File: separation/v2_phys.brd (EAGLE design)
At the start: 8 parts

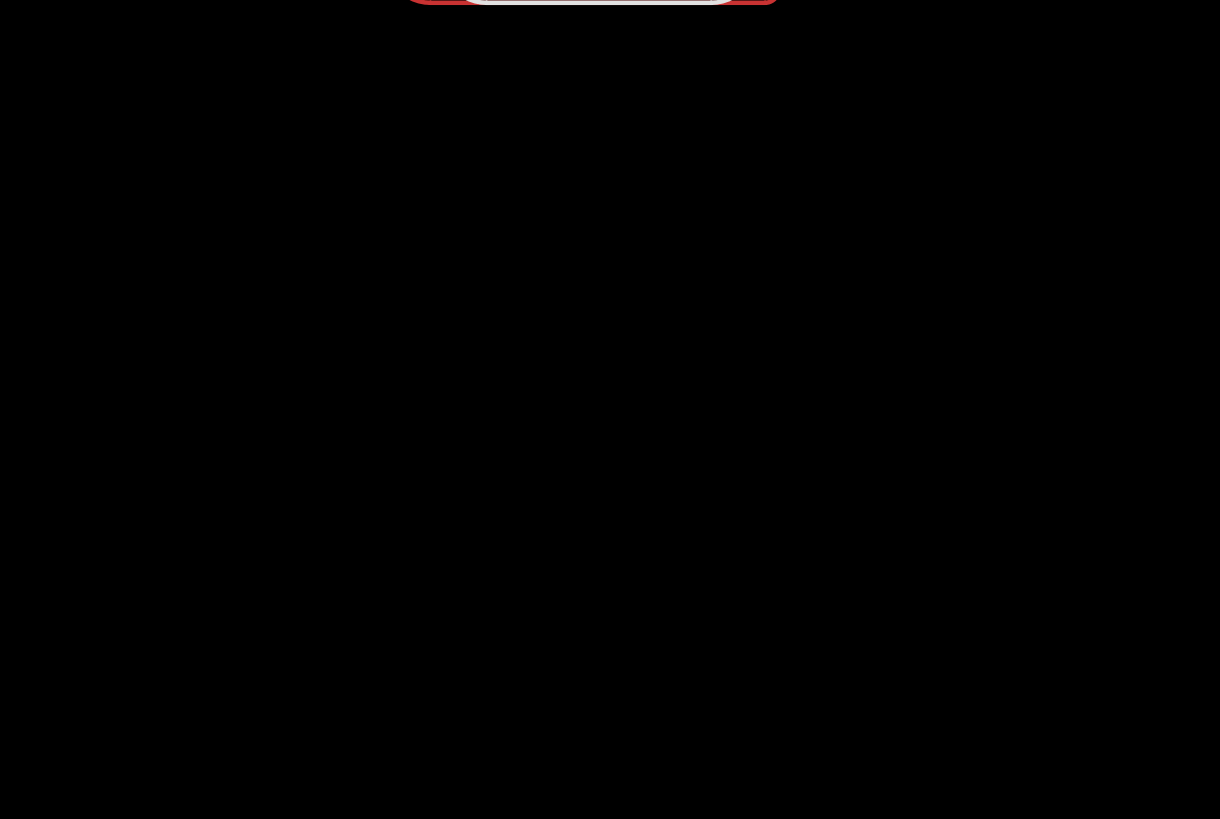
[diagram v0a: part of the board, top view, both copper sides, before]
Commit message: add 3x pressure sensors to physical model
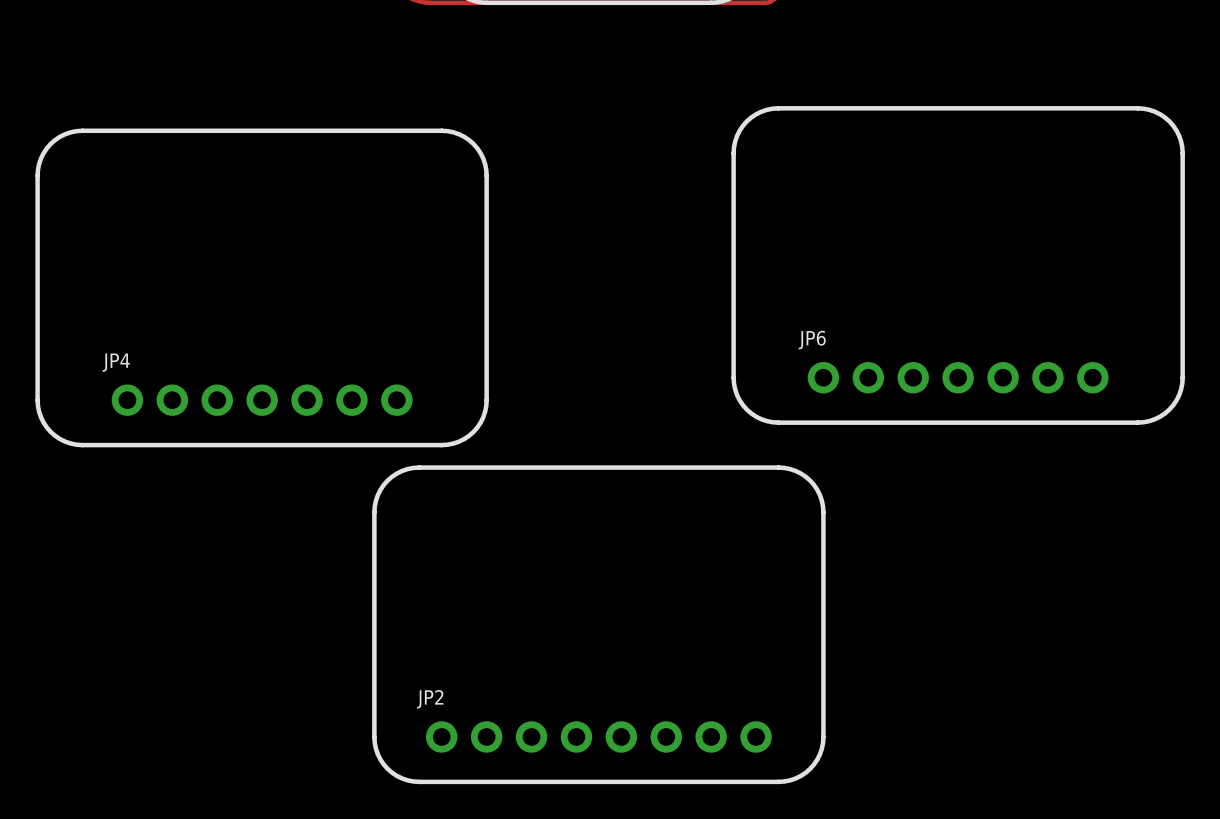
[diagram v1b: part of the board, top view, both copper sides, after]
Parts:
- added JP2: (no value), microbuilder:1X08_ROUND_70
- added JP4, JP6: (no value), microbuilder:1X07_ROUND_70
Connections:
- new net 3.3V: JP2.2, JP4.2, JP6.2
- new net CS: JP2.7, JP4.7, JP6.7
- new net INT: JP2.8
- new net SCK/SCL: JP2.4, JP4.4, JP6.4
- new net SDI/SDA: JP2.6, JP4.6, JP6.6
- new net SDO/ADR: JP2.5, JP4.5, JP6.5
- net GND: now also JP2.3, JP4.3, JP6.3
- net VCC: now also JP2.1, JP4.1, JP6.1
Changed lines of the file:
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@@
 <wire x1="-8.89" y1="26.543" x2="-10.668" y2="26.543" width="1.524" layer="29"/>
 <wire x1="-8.89" y1="29.083" x2="-10.668" y2="29.083" width="1.524" layer="29"/>
+<wire x1="-13.97" y1="-17.78" x2="-13.97" y2="-30.48" width="0.254" layer="21"/>
+<wire x1="-13.97" y1="-30.48" x2="-11.43" y2="-33.02" width="0.254" layer="21" curve="90"/>
+<wire x1="-11.43" y1="-33.02" x2="8.89" y2="-33.02" width="0.254" layer="21"/>
+<wire x1="8.89" y1="-33.02" x2="11.43" y2="-30.48" width="0.254" layer="21" curve="90"/>
+<wire x1="11.43" y1="-30.48" x2="11.43" y2="-17.78" width="0.254" layer="21"/>
+<wire x1="11.43" y1="-17.78" x2="8.89" y2="-15.24" width="0.254" layer="21" curve="90"/>
+<wire x1="8.89" y1="-15.24" x2="-11.43" y2="-15.24" width="0.254" layer="21"/>
+<wire x1="-11.43" y1="-15.24" x2="-13.97" y2="-17.78" width="0.254" layer="21" curve="90"/>
+<wire x1="-33.02" y1="1.27" x2="-33.02" y2="-11.43" width="0.254" layer="21"/>
+<wire x1="-33.02" y1="-11.43" x2="-30.48" y2="-13.97" width="0.254" layer="21" curve="90"/>
+<wire x1="-30.48" y1="-13.97" x2="-10.16" y2="-13.97" width="0.254" layer="21"/>
+<wire x1="-10.16" y1="-13.97" x2="-7.62" y2="-11.43" width="0.254" layer="21" curve="90"/>
+<wire x1="-7.62" y1="-11.43" x2="-7.62" y2="1.27" width="0.254" layer="21"/>
+<wire x1="-7.62" y1="1.27" x2="-10.16" y2="3.81" width="0.254" layer="21" curve="90"/>
+<wire x1="-10.16" y1="3.81" x2="-30.48" y2="3.81" width="0.254" layer="21"/>
+<wire x1="-30.48" y1="3.81" x2="-33.02" y2="1.27" width="0.254" layer="21" curve="90"/>
+<wire x1="6.35" y1="2.54" x2="6.35" y2="-10.16" width="0.254" layer="21"/>
+<wire x1="6.35" y1="-10.16" x2="8.89" y2="-12.7" width="0.254" layer="21" curve="90"/>
+<wire x1="8.89" y1="-12.7" x2="29.21" y2="-12.7" width="0.254" layer="21"/>
+<wire x1="29.21" y1="-12.7" x2="31.75" y2="-10.16" width="0.254" layer="21" curve="90"/>
+<wire x1="31.75" y1="-10.16" x2="31.75" y2="2.54" width="0.254" layer="21"/>
+<wire x1="31.75" y1="2.54" x2="29.21" y2="5.08" width="0.254" layer="21" curve="90"/>
+<wire x1="29.21" y1="5.08" x2="8.89" y2="5.08" width="0.254" layer="21"/>
+<wire x1="8.89" y1="5.08" x2="6.35" y2="2.54" width="0.254" layer="21" curve="90"/>
 </plain>
 <attributes>
@@
 <class number="0" name="default" width="0" drill="0">
 </class>
-<class number="1" name="power" width="0.3048" drill="0">
+<class number="1" name="highpower" width="0.3048" drill="0.4826">
+</class>
+<class number="2" name="lowpower" width="0.3048" drill="0.4826">
 </class>
 </classes>
@@
 <attribute name="VALUE" x="8.1534" y="31.1404" size="0.9906" layer="27" ratio="10"/>
 </element>
+<element name="JP2" library="microbuilder" package="1X08_ROUND_70" value="" x="-1.27" y="-30.48" smashed="yes">
+<attribute name="NAME" x="-11.5062" y="-28.6512" size="0.8128" layer="25" ratio="18"/>
+<attribute name="VALUE" x="-11.43" y="-33.655" size="0.4064" layer="27" ratio="10"/>
+</element>
+<element name="JP4" library="microbuilder" package="1X07_ROUND_70" value="" x="-20.32" y="-11.43" smashed="yes">
+<attribute name="NAME" x="-29.2862" y="-9.6012" size="0.8128" layer="25" ratio="18"/>
+<attribute name="VALUE" x="-29.21" y="-14.605" size="0.4064" layer="27" ratio="10"/>
+</element>
+<element name="JP6" library="microbuilder" package="1X07_ROUND_70" value="" x="19.05" y="-10.16" smashed="yes">
+<attribute name="NAME" x="10.0838" y="-8.3312" size="0.8128" layer="25" ratio="18"/>
+<attribute name="VALUE" x="10.16" y="-13.335" size="0.4064" layer="27" ratio="10"/>
+</element>
 </elements>
 <signals>
@@
 <contactref element="LOUD" pad="2"/>
 <contactref element="R2" pad="2"/>
+<contactref element="JP2" pad="3"/>
+<contactref element="JP4" pad="3"/>
+<contactref element="JP6" pad="3"/>
+<wire x1="11.303" y1="27.051" x2="14.097" y2="22.931" width="0" layer="19" extent="1-1"/>
 <wire x1="13.97" y1="13.97" x2="14.097" y2="22.931" width="0" layer="19" extent="1-1"/>
-<wire x1="-17.79" y1="17.018" x2="13.97" y2="13.97" width="0" layer="19" extent="1-1"/>
+<wire x1="-8.89" y1="16.3195" x2="11.303" y2="27.051" width="0" layer="19" extent="1-1"/>
+<wire x1="-17.79" y1="17.018" x2="-8.89" y2="16.3195" width="0" layer="19" extent="1-1"/>
 <wire x1="-17.78" y1="22.67" x2="-17.79" y2="17.018" width="0" layer="19" extent="1-1"/>
-<wire x1="11.303" y1="27.051" x2="-17.78" y2="22.67" width="0" layer="19" extent="1-1"/>
-<wire x1="-8.89" y1="16.3195" x2="11.303" y2="27.051" width="0" layer="19" extent="1-1"/>
+<wire x1="16.51" y1="-10.16" x2="13.97" y2="13.97" width="0" layer="19" extent="1-1"/>
+<wire x1="-22.86" y1="-11.43" x2="-17.79" y2="17.018" width="0" layer="19" extent="1-1"/>
+<wire x1="-5.08" y1="-30.48" x2="-22.86" y2="-11.43" width="0" layer="19" extent="1-1"/>
 </signal>
 <signal name="MOSI">
@@
 <wire x1="-20.32" y1="15.24" x2="-18.8595" y2="13.7795" width="0.508" layer="16" curve="90"/>
 <wire x1="-18.8595" y1="13.7795" x2="-8.89" y2="13.7795" width="0.508" layer="16"/>
+<contactref element="JP2" pad="1"/>
+<contactref element="JP4" pad="1"/>
+<contactref element="JP6" pad="1"/>
+<wire x1="-27.94" y1="-11.43" x2="-10.16" y2="-30.48" width="0" layer="19" extent="1-1"/>
+<wire x1="-20.34" y1="17.018" x2="-27.94" y2="-11.43" width="0" layer="19" extent="1-1"/>
+<wire x1="11.43" y1="-10.16" x2="-10.16" y2="-30.48" width="0" layer="19" extent="1-1"/>
 </signal>
 <signal name="+3V3">
@@
 <wire x1="9.652" y1="28.829" x2="9.652" y2="19.812" width="0.254" layer="1"/>
 </signal>
+<signal name="3.3V">
+<contactref element="JP2" pad="2"/>
+<contactref element="JP4" pad="2"/>
+<contactref element="JP6" pad="2"/>
+<wire x1="-25.4" y1="-11.43" x2="-7.62" y2="-30.48" width="0" layer="19" extent="1-1"/>
+<wire x1="13.97" y1="-10.16" x2="-7.62" y2="-30.48" width="0" layer="19" extent="1-1"/>
+</signal>
+<signal name="SDO/ADR">
+<contactref element="JP2" pad="5"/>
+<contactref element="JP4" pad="5"/>
+<contactref element="JP6" pad="5"/>
+<wire x1="-17.78" y1="-11.43" x2="0" y2="-30.48" width="0" layer="19" extent="1-1"/>
+<wire x1="21.59" y1="-10.16" x2="0" y2="-30.48" width="0" layer="19" extent="1-1"/>
+</signal>
+<signal name="SDI/SDA">
+<contactref element="JP2" pad="6"/>
+<contactref element="JP4" pad="6"/>
+<contactref element="JP6" pad="6"/>
+<wire x1="-15.24" y1="-11.43" x2="2.54" y2="-30.48" width="0" layer="19" extent="1-1"/>
+<wire x1="24.13" y1="-10.16" x2="2.54" y2="-30.48" width="0" layer="19" extent="1-1"/>
+</signal>
+<signal name="SCK/SCL">
+<contactref element="JP2" pad="4"/>
+<contactref element="JP4" pad="4"/>
+<contactref element="JP6" pad="4"/>
+<wire x1="-20.32" y1="-11.43" x2="-2.54" y2="-30.48" width="0" layer="19" extent="1-1"/>
+<wire x1="19.05" y1="-10.16" x2="-2.54" y2="-30.48" width="0" layer="19" extent="1-1"/>
+</signal>
+<signal name="CS">
+<contactref element="JP2" pad="7"/>
+<contactref element="JP4" pad="7"/>
+<contactref element="JP6" pad="7"/>
+<wire x1="-12.7" y1="-11.43" x2="5.08" y2="-30.48" width="0" layer="19" extent="1-1"/>
+<wire x1="26.67" y1="-10.16" x2="5.08" y2="-30.48" width="0" layer="19" extent="1-1"/>
+</signal>
+<signal name="INT">
+<contactref element="JP2" pad="8"/>
+</signal>
 </signals>

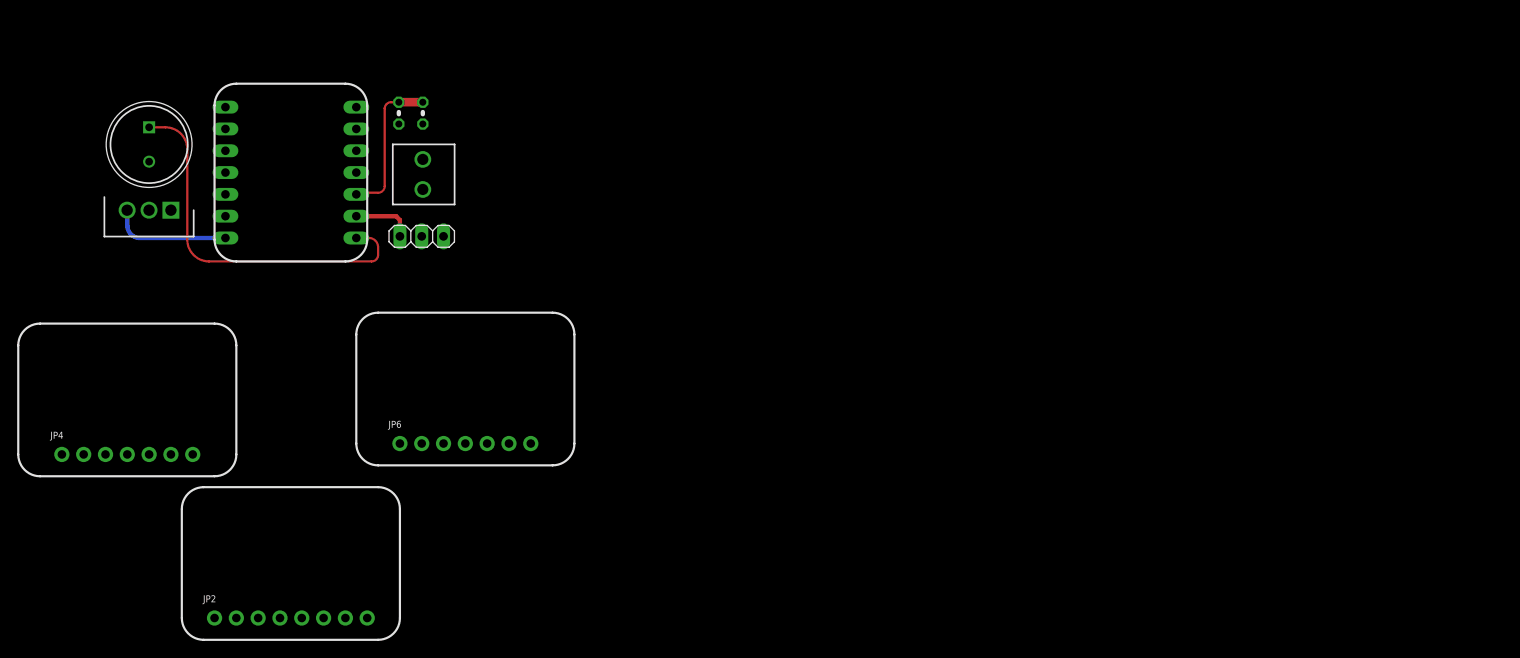
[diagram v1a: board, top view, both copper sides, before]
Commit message: possible physical layout
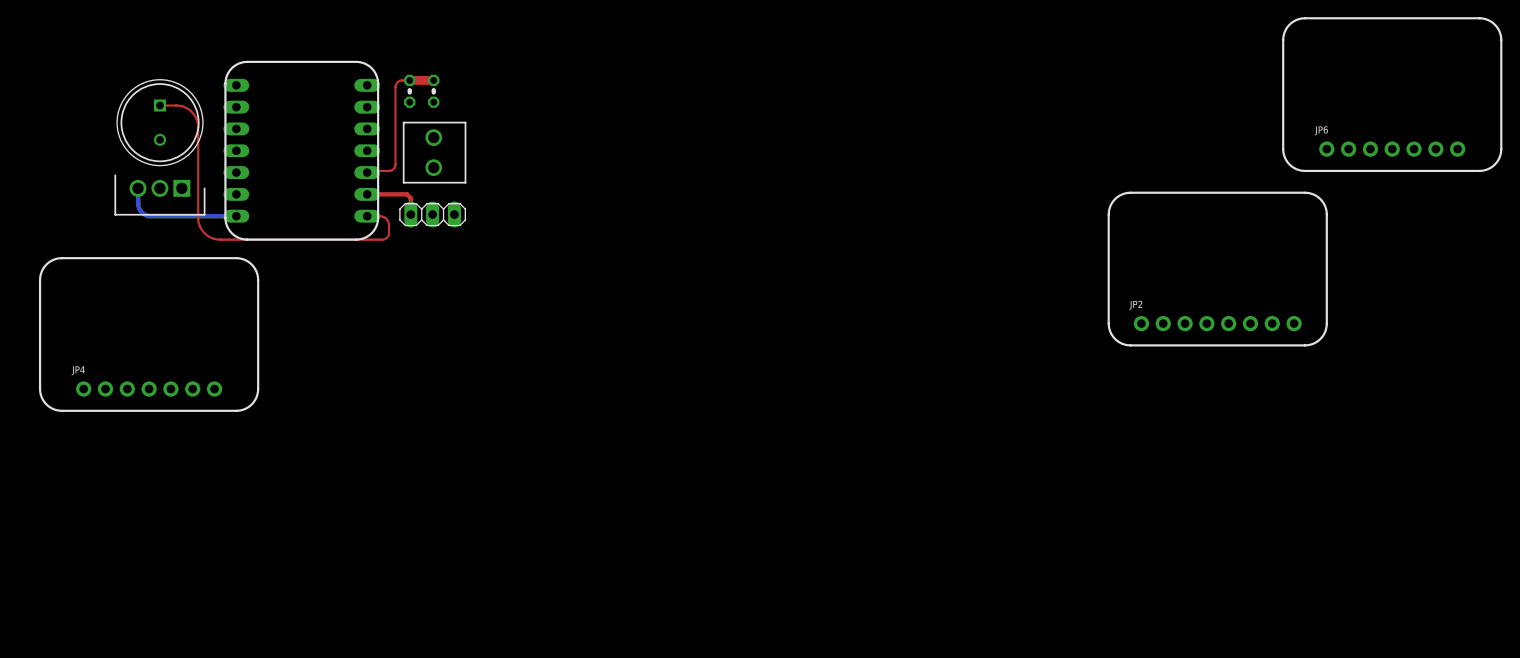
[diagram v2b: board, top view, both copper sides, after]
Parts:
- moved JP2 113.3 mm to (106.7, 3.81)
- moved JP6 113.3 mm to (127.0, 24.1)
- moved JP4 8.03 mm to (-17.8, -3.81)
- moved SERCON 2.84 mm to (15.2, 16.5)
- moved BAT 2.84 mm to (15.4, 22.0)
- moved MCU-L 2.84 mm to (7.62, 23.9)
- moved MCU-R 2.84 mm to (-7.62, 23.9)
- moved R1 2.84 mm to (15.4, 30.9)
- moved LDO 2.84 mm to (-14.0, 19.6)
- moved LOUD 2.84 mm to (-16.5, 29.2)
- moved R2 2.84 mm to (12.6, 30.9)

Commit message: update physical map with updated board
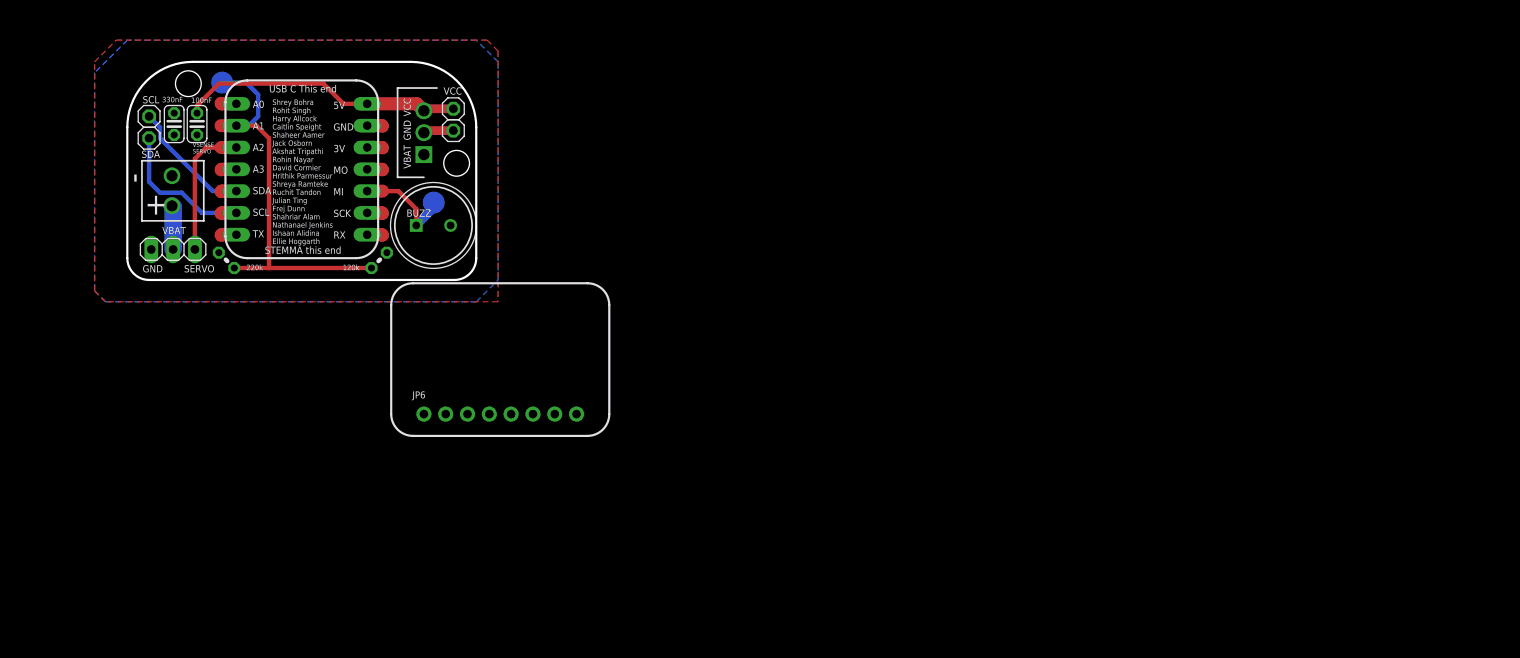
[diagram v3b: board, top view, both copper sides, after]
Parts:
- added C1: 100nF, rcl:C025-024X044
- added C2: 330nF, rcl:C025-024X044
- added JP1, JP3: (no value), pinhead:1X01
- added TP2, TP6: TPSQB2,54, testpad:B2,54
- JP2: device microbuilder:1X08_ROUND_70 -> pinhead:1X01
- JP4: device microbuilder:1X07_ROUND_70 -> pinhead:1X01
- JP6: device microbuilder:1X07_ROUND_70 -> microbuilder:1X08_ROUND_70
- moved JP2 126.8 mm to (-17.8, 27.9)
- moved JP6 108.4 mm to (23.1, -6.73)
- moved JP4 48.2 mm to (17.7, 28.8)
- moved LOUD 33.0 mm to (13.3, 15.2), turned to 0 degrees
- moved R1 31.1 mm to (-8.76, 11.2), turned to 315 degrees
- moved BAT 30.8 mm to (-15.1, 17.5)
- moved SERCON 30.5 mm to (-15.0, 12.4), turned to 0 degrees
- moved LDO 28.5 mm to (14.2, 23.5), turned to 90 degrees
- moved R2 20.0 mm to (9.02, 11.2), turned to 45 degrees
- moved MCU-L 15.4 mm to (-7.62, 21.8), turned to 270 degrees
- moved MCU-R 15.4 mm to (7.62, 21.8), turned to 90 degrees
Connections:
- removed net MISO: MCU-R.3
- new net A0: MCU-L.1
- net 3.3V: no longer JP2.2, JP4.2
- net BUZZ: now also MCU-R.3, TP6.TP; no longer MCU-L.1
- net CS: no longer JP2.7, JP4.7
- net GND: now also C1.1, C2.1, JP1.1, SERCON.1; no longer JP2.3, JP4.3, SERCON.2
- net INT: now also JP6.8; no longer JP2.8
- net SCK/SCL: no longer JP2.4, JP4.4
- net SCL: now also JP3.1
- net SDA: now also JP2.1
- net SDI/SDA: no longer JP2.6, JP4.6
- net SDO/ADR: no longer JP2.5, JP4.5
- net SERVO: now also MCU-L.3; no longer MCU-L.2
- net VBAT: now also C2.2, SERCON.2; no longer SERCON.1
- net VCC: now also C1.2; no longer JP2.1
- net VSENSE: now also MCU-L.2, TP2.TP; no longer MCU-L.3
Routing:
- net BUZZ: track 43.5 -> 12.0 mm
- net VSENSE: track 17.5 -> 47.8 mm
- net VCC: track 13.8 -> 33.2 mm
- net SCL: track 0.00 -> 18.5 mm
- net SDA: track 0.00 -> 16.3 mm
- net SERVO: track 7.17 -> 15.9 mm
- net GND: track 0.00 -> 5.33 mm
- net VBAT: track 0.00 -> 5.13 mm
- net TX: track 0.00 -> 1.80 mm
- net SCK: track 0.00 -> 1.80 mm
- net RX: track 0.00 -> 1.80 mm
- net MOSI: track 0.00 -> 1.80 mm
- net A3: track 0.00 -> 1.80 mm
- net A0: track 0.00 -> 1.80 mm
- net +3V3: track 0.00 -> 1.80 mm
- added copper zone on layer 16, net GND
- added copper zone on layer 1, net VBAT
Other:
- board outline added: 40.6 x 25.4 mm
- board text added: "+"
- board text added: "-"
- board text added: "5V GND 3V MO MI SCK RX"
- board text added: "A0 A1 A2 A3 SDA SCL TX"
- board text added: "ART Separation"
- board text added: "ASTRA Designed by ART@ICLR"
- board text added: "Akshat Tripathi"
- board text added: "BUZZ"
- board text added: "David Cormier"
- board text added: "Designed by"
- board text added: "GND"
- board text added: "Hrithik Parmessur"
- board text added: "Ruchit Tandon"
- board text added: "SCL"
- board text added: "SDA"
- board text added: "SERVO"
- board text added: "STEMMA this end"
- board text added: "Shrey Bohra"
- board text added: "Shrey Bohra Rohit Singh Harry Allcock Caitlin Speight Shaheer Aamer Jack Osborn Akshat Tripathi Rohin Nayar David Cormier Hrithik Parmessur Shreya Ramteke Ruchit Tandon Julian Ting Frej Dunn Shahriar Alam Nathanael Jenkins Ishaan Alidina Ellie Hoggarth"
- board text added: "Shreya Ramteke"
- board text added: "USB C This end"
- board text added: "VBAT"
- board text added: "VCC"
- board text added: "VSENSE"
- board text added: "VSENSE SERVO"
